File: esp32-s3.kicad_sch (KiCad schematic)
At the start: 14 parts, among them J4 Conn_01x05, SW1 RESET, SW2 BOOT, U3 ESP32-S3-WROOM-1

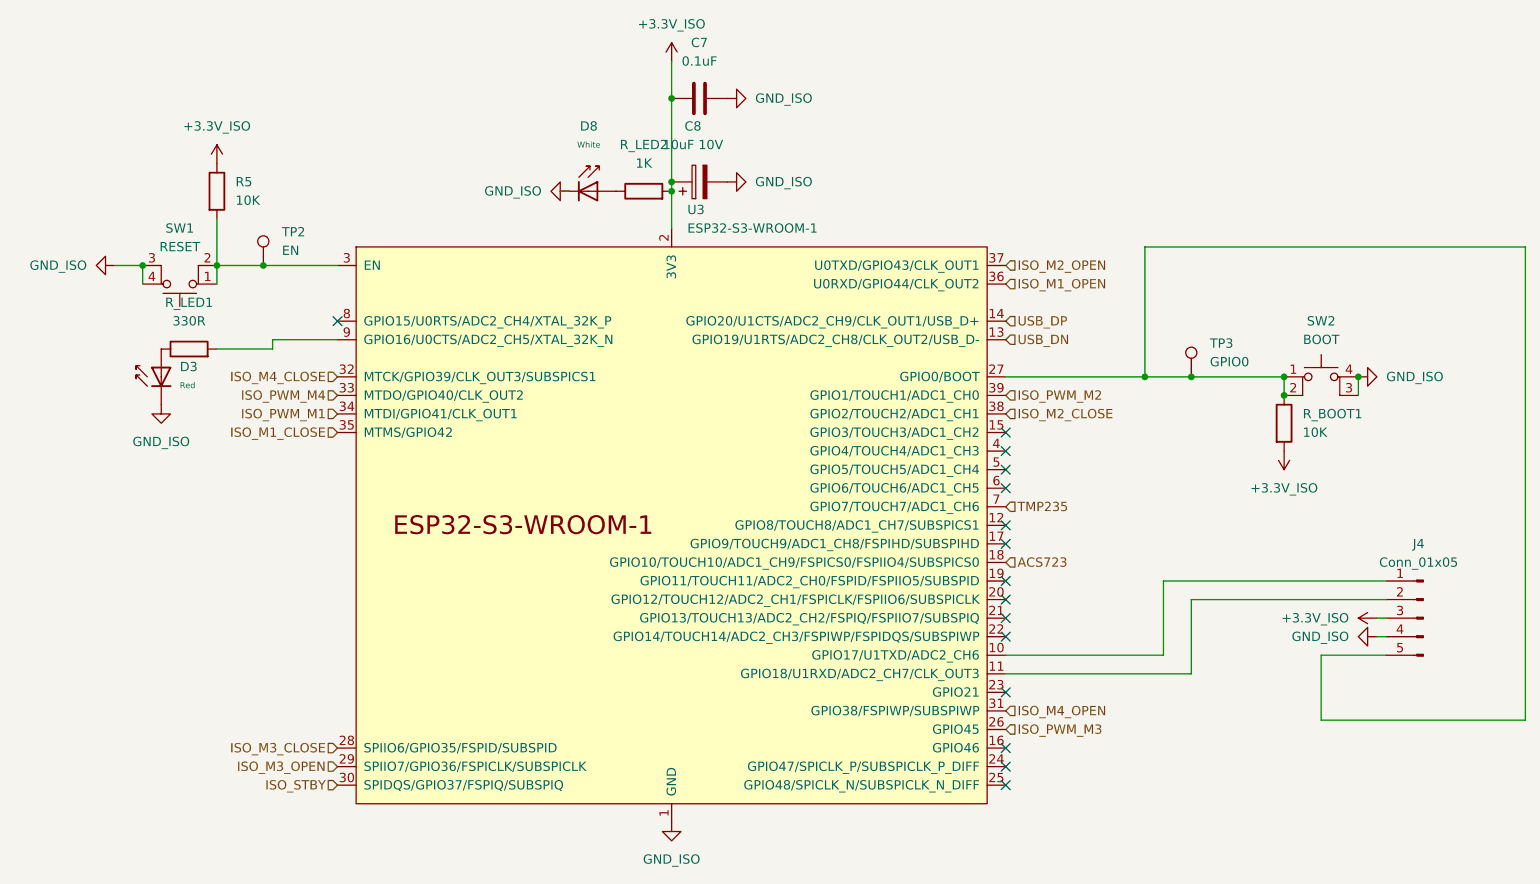
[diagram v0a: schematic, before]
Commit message: Updating routing with new terminal block
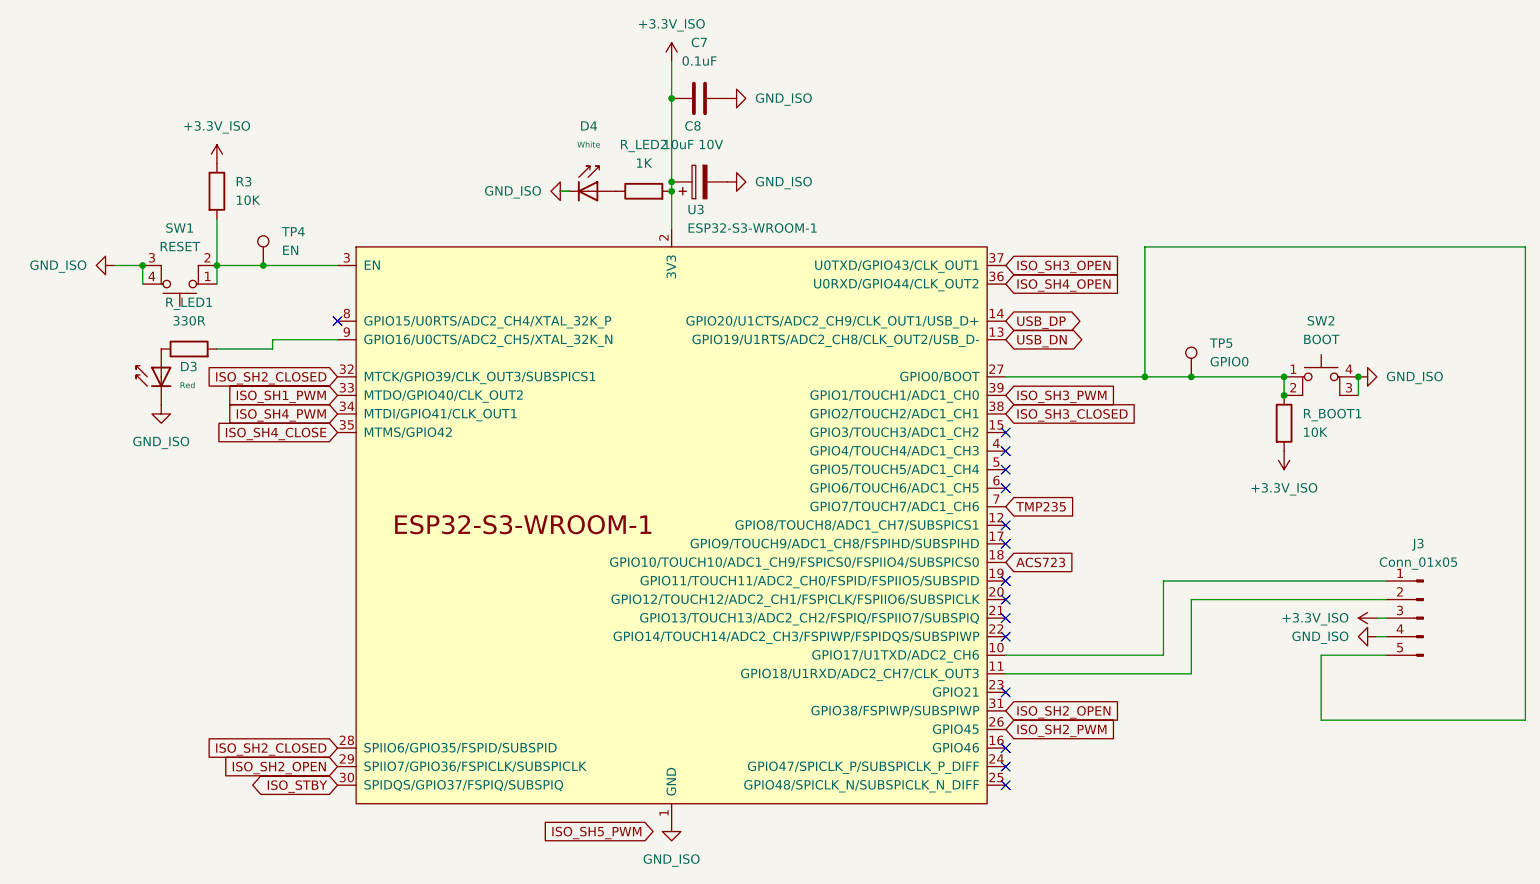
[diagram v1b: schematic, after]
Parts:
- D3: footprint PCM_JLCPCB:D_0805 -> Diode_SMD:D_0805_2012Metric
- D4: renamed from D8; footprint PCM_JLCPCB:D_0805 -> Diode_SMD:D_0805_2012Metric
- TP4: renamed from TP2; footprint barn_shade_controller:TestPoint_Pad_D1.0mm_No_SolderMask -> TestPoint:TestPoint_Pad_D1.0mm
- TP5: renamed from TP3; footprint barn_shade_controller:TestPoint_Pad_D1.0mm_No_SolderMask -> TestPoint:TestPoint_Pad_D1.0mm
- U3: footprint PCM_Espressif:ESP32-S3-WROOM-1 -> Espressif:ESP32-S3-WROOM-1
- renumbered J4 to J3, R5 to R3
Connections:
- net ISO_M4_CLOSE is gone; now on net ISO_SH2_CLOSED: U3.32 (MTCK/GPIO39/CLK_OUT3/SUBSPICS1)
- net ISO_M4_OPEN is gone; now on net ISO_SH2_OPEN: U3.31 (GPIO38/FSPIWP/SUBSPIWP)
- net ISO_M1_CLOSE renamed ISO_SH4_CLOSE
- net ISO_M1_OPEN renamed ISO_SH4_OPEN
- net ISO_M2_CLOSE renamed ISO_SH3_CLOSED
- net ISO_M2_OPEN renamed ISO_SH3_OPEN
- net ISO_M3_CLOSE renamed ISO_SH2_CLOSED
- net ISO_M3_OPEN renamed ISO_SH2_OPEN
- net ISO_PWM_M1 renamed ISO_SH4_PWM
- net ISO_PWM_M2 renamed ISO_SH3_PWM
- net ISO_PWM_M3 renamed ISO_SH2_PWM
- net ISO_PWM_M4 renamed ISO_SH1_PWM

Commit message: Adding switches to PCB
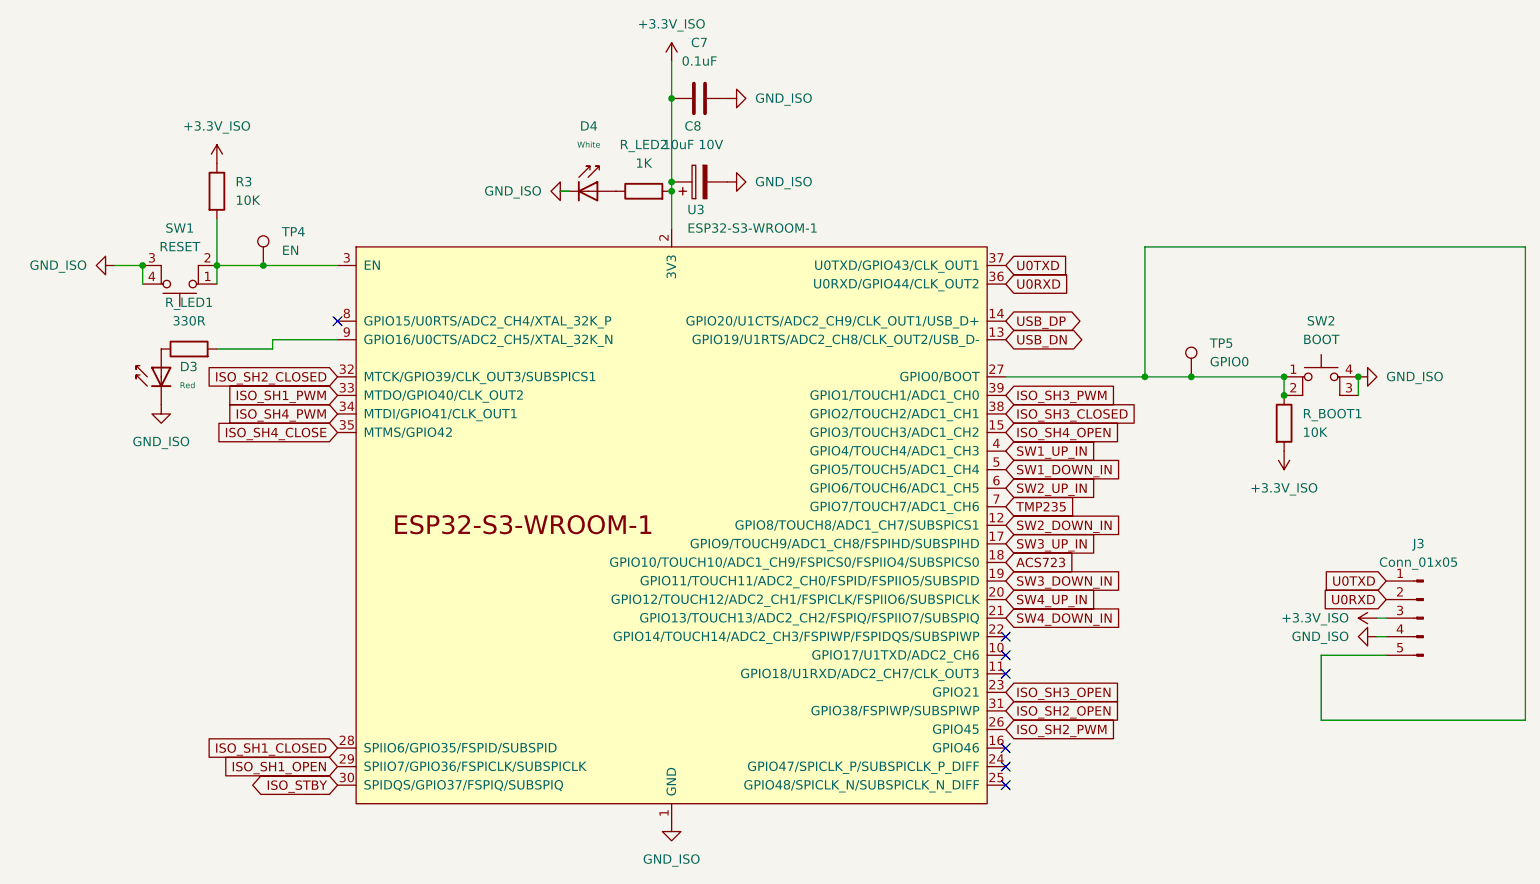
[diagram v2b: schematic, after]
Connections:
- net ISO_SH2_CLOSED: no longer U3.28 (SPIIO6/GPIO35/FSPID/SUBSPID)
- net ISO_SH2_OPEN: no longer U3.29 (SPIIO7/GPIO36/FSPICLK/SUBSPICLK)
- net ISO_SH3_OPEN: now also U3.23 (GPIO21); no longer U3.37 (U0TXD/GPIO43/CLK_OUT1)
- net ISO_SH4_OPEN: now also U3.15 (GPIO3/TOUCH3/ADC1_CH2); no longer U3.36 (U0RXD/GPIO44/CLK_OUT2)
- net at U3.10 (GPIO17/U1TXD/ADC2_CH6): no longer J3.1 (Pin_1)
- net at U3.11 (GPIO18/U1RXD/ADC2_CH7/CLK_OUT3): no longer J3.2 (Pin_2)
- net SW2_DOWN_IN: now reaches U3.12 (GPIO8/TOUCH8/ADC1_CH7/SUBSPICS1)
- net SW3_UP_IN: now reaches U3.17 (GPIO9/TOUCH9/ADC1_CH8/FSPIHD/SUBSPIHD)
- net SW3_DOWN_IN: now reaches U3.19 (GPIO11/TOUCH11/ADC2_CH0/FSPID/FSPIIO5/SUBSPID)
- net SW4_UP_IN: now reaches U3.20 (GPIO12/TOUCH12/ADC2_CH1/FSPICLK/FSPIIO6/SUBSPICLK)
- net SW4_DOWN_IN: now reaches U3.21 (GPIO13/TOUCH13/ADC2_CH2/FSPIQ/FSPIIO7/SUBSPIQ)
- net SW1_UP_IN: now reaches U3.4 (GPIO4/TOUCH4/ADC1_CH3)
- net SW1_DOWN_IN: now reaches U3.5 (GPIO5/TOUCH5/ADC1_CH4)
- net SW2_UP_IN: now reaches U3.6 (GPIO6/TOUCH6/ADC1_CH5)
- new net ISO_SH1_CLOSED: U3.28 (SPIIO6/GPIO35/FSPID/SUBSPID)
- new net ISO_SH1_OPEN: U3.29 (SPIIO7/GPIO36/FSPICLK/SUBSPICLK)
- new net U0RXD: J3.2 (Pin_2), U3.36 (U0RXD/GPIO44/CLK_OUT2)
- new net U0TXD: J3.1 (Pin_1), U3.37 (U0TXD/GPIO43/CLK_OUT1)
- no-connect marks 15 -> 7
